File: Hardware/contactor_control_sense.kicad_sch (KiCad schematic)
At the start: 52 parts, among them J10 ContactorConnector, J11 ContactorConnector, J4 ContactorConnector, J9 ContactorConnector, Q4 PSMN8R5-40MSDX, Q5 PSMN8R5-40MSDX, Q6 PSMN8R5-40MSDX, Q7 PSMN8R5-40MSDX, SW3 SW_Push_Open, SW4 SW_Push_Open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

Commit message: BPS-Leader Schematic completed (mostly)
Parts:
- removed R31, R35, R42: 10k, Resistor_SMD:R_0603_1608Metric, symbol Device:R_US
- removed SW3, SW4, SW5, SW6: SW_Push_Open, symbol Switch:SW_Push_Open
- added J12, J14, J15: Conn_01x02, symbol Connector_Generic:Conn_01x02
- added Q10, Q8, Q9: PMV213SN,215, Package_TO_SOT_SMD:SOT-23-3, symbol Transistor_FET:BUK7M27-80EX
- added R50, R54: 10k, Resistor_SMD:R_0603_1608Metric, symbol Device:R_US
- D5, D6, D8, D9: footprint UTSVT_Passive:MMDL101T1G -> UTSVT_Passives:MMDL101T1G
- Q4, Q5, Q6, Q7: value PSMN8R5-40MSDX -> PMV213SN,215; footprint Package_TO_SOT_SMD:LFPAK33 -> Package_TO_SOT_SMD:SOT-23-3
- renumbered HV+ to HV+4
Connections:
- net +24V: now also J12.1 (Pin_1); no longer D6.1 (K), R32.2
- net +3.3V: now also Q7.5 (D), Q10.5 (D), Q8.5 (D)
- net ARRAY_CONTROL: now also R29.2, Q9.4 (G); no longer R43.2
- net ARRAY_PRE_CONTROL: now also Q4.4 (G), R39.2
- net GND: now also R43.2, Q9.1 (S), Q9.2 (S), Q9.3 (S), R50.2, R54.2; no longer Q7.1 (S), Q7.2 (S), Q7.3 (S), R43.1
- net HV+_CONTROL: now also Q5.4 (G), R44.2
- net HV-_CONTROL: now also Q6.4 (G), R45.2
- net at Q7.4 (G): now also D6.1 (K), R32.2, J15.2 (Pin_2); no longer R39.2
- net ARRAY_PRE_SENSE- renamed ARRAY_PRE_CONTROL-
- net ARRAY_PRE_CONTROL-: now also Q4.5 (D); no longer Q7.5 (D)
- net ARRAY_SENSE- renamed ARRAY_CONTROL-
- net ARRAY_CONTROL-: now also Q9.5 (D); no longer Q4.5 (D)
- net HV+_SENSE- renamed HV+_CONTROL-
- net HV-_SENSE- renamed HV-_CONTROL-
- new net: J12.2 (Pin_2), J14.1 (Pin_1), Q10.4 (G)
- new net: J14.2 (Pin_2), J15.1 (Pin_1), Q8.4 (G)
- new net ESTOP_1: Q10.1 (S), Q10.2 (S), Q10.3 (S), R43.1
- new net ESTOP_2: Q8.1 (S), Q8.2 (S), Q8.3 (S), R50.1
- new net ESTOP_3: Q7.1 (S), Q7.2 (S), Q7.3 (S), R54.1
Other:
- note removed: "I was recently informed that this may have to go on 4 seperate sheets In addition, I fear I might have implemented "estop button in series" too literally"
- moved on the sheet: C15, C16, C17, C19, C22, C23, D6, D8, D9, HV+1, HV+2, HV+3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

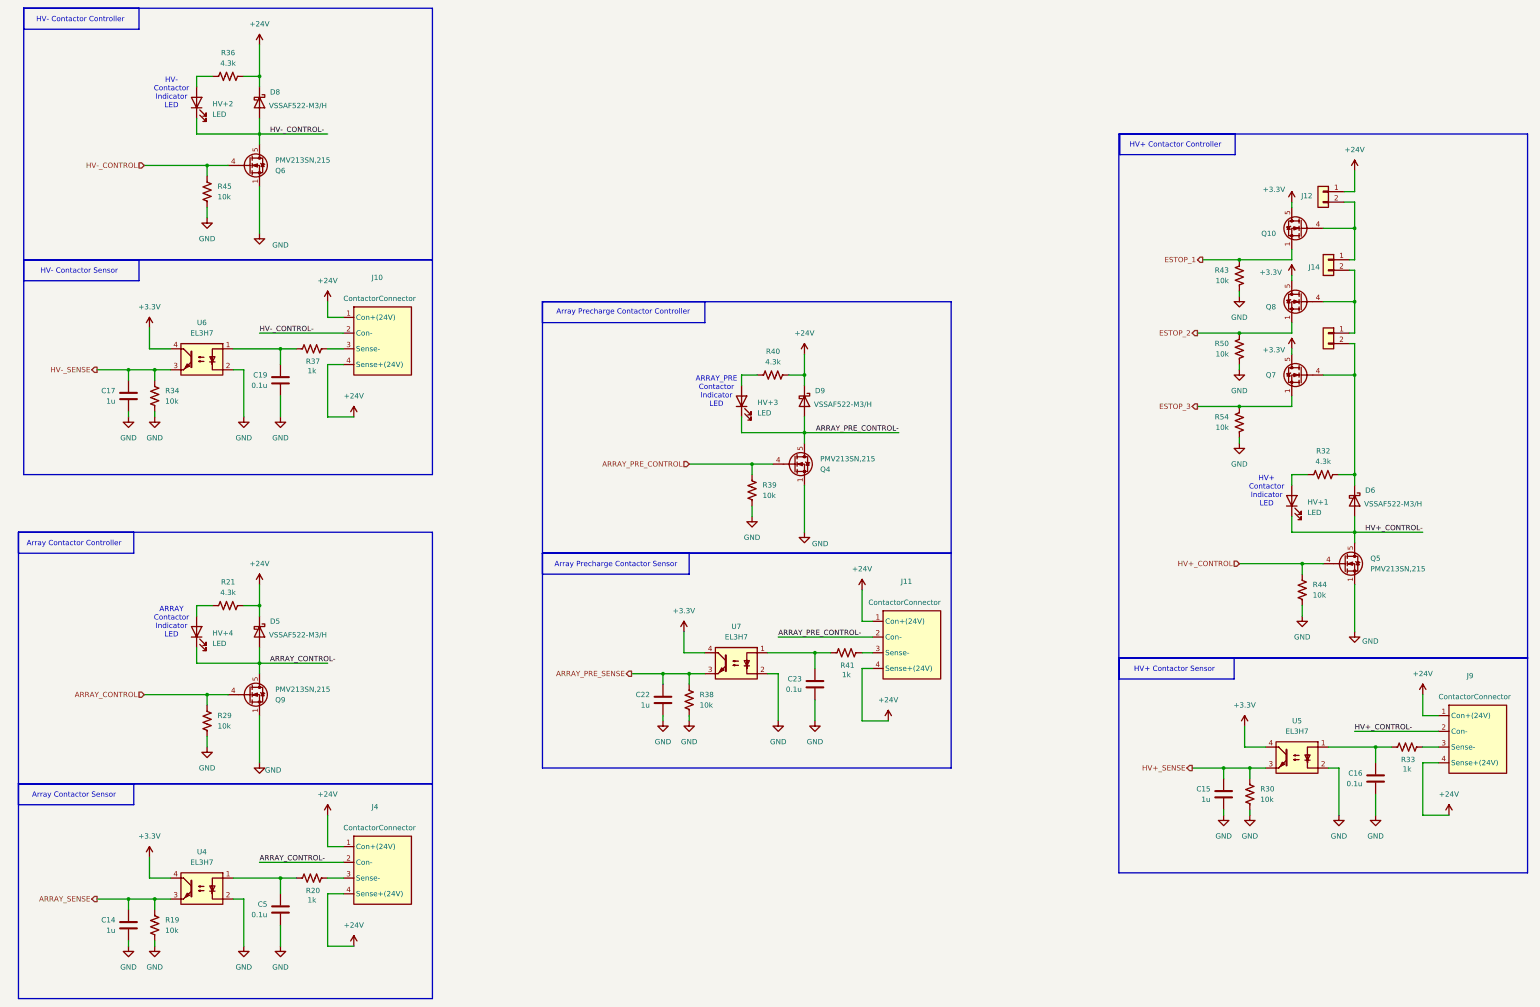
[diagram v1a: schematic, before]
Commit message: added fuse, made kiCad Sharepoint a submodule, added a pulldown, added test-points
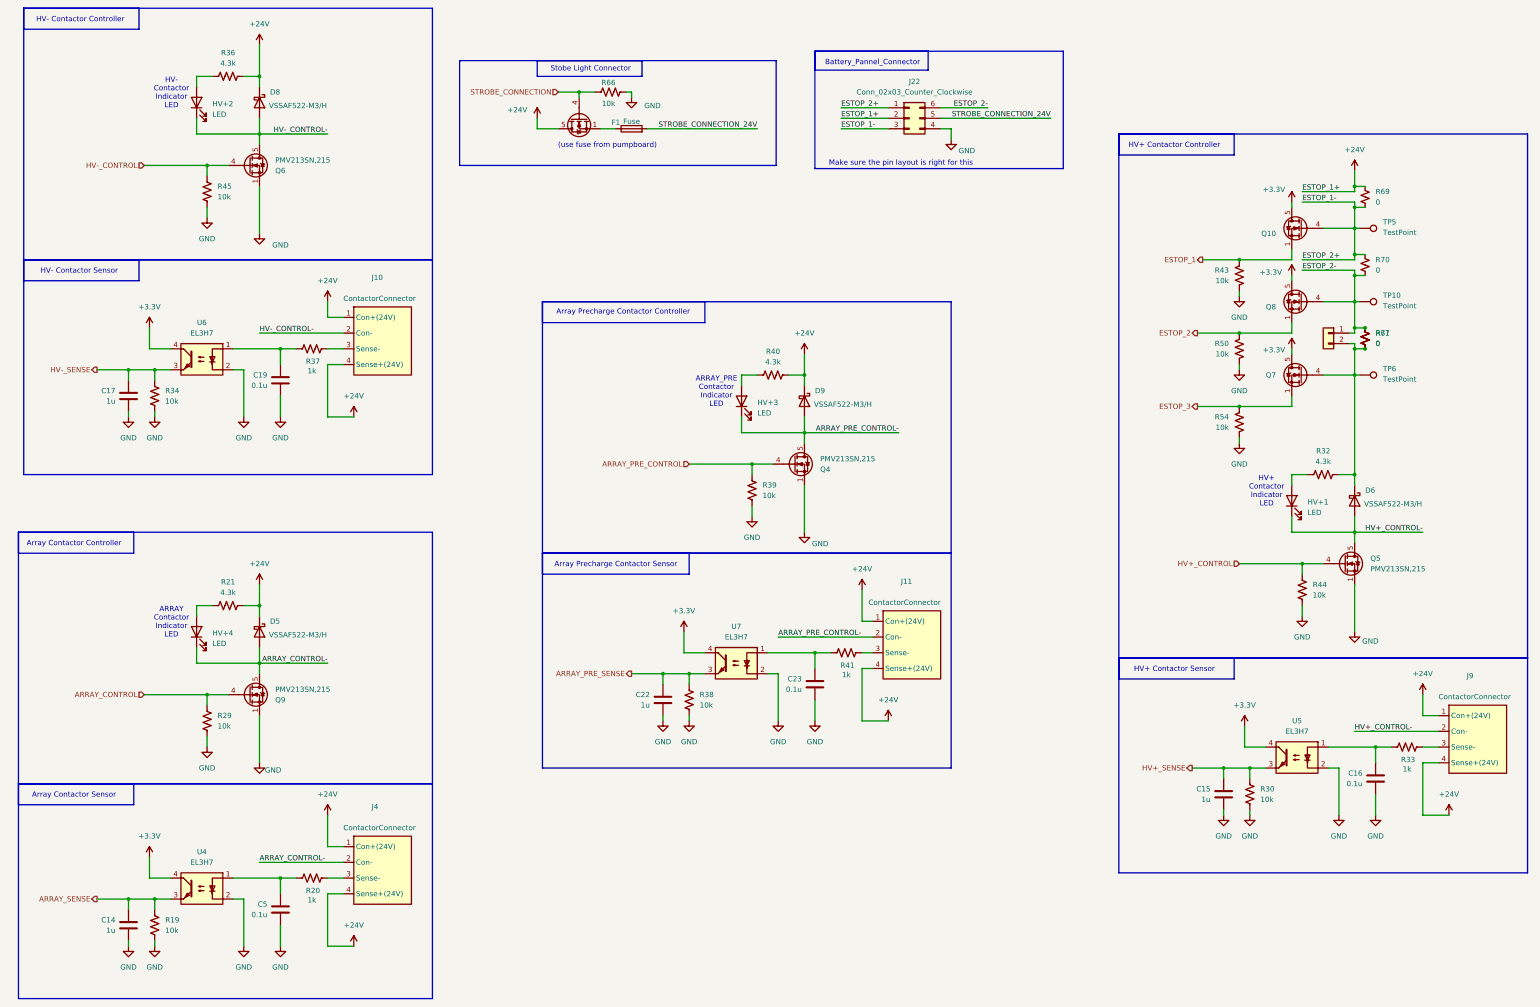
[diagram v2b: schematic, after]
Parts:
- removed J12, J14: Conn_01x02, symbol Connector_Generic:Conn_01x02
- added F1: Fuse, symbol Device:Fuse
- added J22: Conn_02x03_Counter_Clockwise, symbol Connector_Generic:Conn_02x03_Counter_Clockwise
- added Q11: PMV213SN,215, Package_TO_SOT_SMD:SOT-23-3, symbol Transistor_FET:BUK7M27-80EX
- added R66: 10k, Resistor_SMD:R_0603_1608Metric, symbol Device:R_US
- added R67, R69, R70, R71: 0, symbol Device:R_Small_US
- added TP10, TP5, TP6: TestPoint, symbol Connector:TestPoint
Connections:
- net +24V: now also J22.2 (Pin_2), Q11.5 (D), R69.1
- net GND: now also J22.4 (Pin_4), R66.2
- net ESTOP_1-: now reaches Q10.4 (G)
- net ESTOP_1-: now also J22.1 (Pin_1), J22.3 (Pin_3), R69.2, R70.1, TP5.1
- net at D6.1 (K), J15.2 (Pin_2), Q7.4 (G)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: now also R67.2, R71.2, TP6.1
- net ESTOP_2-: now reaches J15.1 (Pin_1), Q8.4 (G)
- net ESTOP_2-: now also J22.6 (Pin_6), R67.1, R70.2, R71.1, TP10.1
- new net: F1.1, Q11.1 (S), Q11.2 (S), Q11.3 (S)
- new net STROBE_CONNECTION: Q11.4 (G), R66.1
- new net STROBE_CONNECTION_24V: F1.2, J22.5 (Pin_5)
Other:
- note added: "(use fuse from pumpboard)"
- note added: "Battery_Pannel_Connector"
- note added: "Make sure the pin layout is right for this"
- note added: "Stobe Light Connector"

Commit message: Small tweaks
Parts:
- removed R67: 0, symbol Device:R_Small_US
- added TP34, TP36, TP37, TP38, TP39, TP40, TP41, TP42, TP43, TP44, TP45, TP7, TP8, TP9: TestPoint, UTSVT_Special:TestPoint_HEX_3mmID, symbol Connector:TestPoint
- R69, R70, R71: footprint (none) -> Resistor_SMD:R_0603_1608Metric; now not fitted
- TP10, TP5, TP6: footprint (none) -> UTSVT_Special:TestPoint_HEX_3mmID
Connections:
- net ARRAY_CONTROL: now also TP38.1
- net ARRAY_CONTROL-: now also TP34.1
- net ARRAY_PRE_CONTROL: now also TP42.1
- net ARRAY_PRE_CONTROL-: now also TP9.1
- net ARRAY_PRE_SENSE: now also TP41.1
- net ARRAY_SENSE: now also TP40.1
- net HV+_CONTROL: now also TP45.1, TP8.1
- net HV+_CONTROL-: now also TP7.1
- net HV+_SENSE: now also TP44.1
- net HV-_CONTROL: now also TP39.1
- net HV-_CONTROL-: now also TP36.1
- net HV-_SENSE: now also TP37.1
- net STROBE_CONNECTION_24V: now also TP43.1
- net ESTOP_1- renamed ESTOP_1-,2+
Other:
- moved on the sheet: Q10, Q7, Q8

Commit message: Very, very intial layout designed. Many issues. Too bad!
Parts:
- removed F1: Fuse, symbol Device:Fuse
- removed J22: Conn_02x03_Counter_Clockwise, symbol Connector_Generic:Conn_02x03_Counter_Clockwise
- removed Q11: PMV213SN,215, Package_TO_SOT_SMD:SOT-23-3, symbol Transistor_FET:BUK7M27-80EX
- removed R66: 10k, Resistor_SMD:R_0603_1608Metric, symbol Device:R_US
- removed TP43, TP8: TestPoint, UTSVT_Special:TestPoint_HEX_3mmID, symbol Connector:TestPoint
- J15: footprint (none) -> Connector_Molex:Molex_Nano-Fit_105309-xx02_1x02_P2.50mm_Vertical
- TP10, TP34, TP36, TP37, TP38, TP39, TP40, TP41, TP42, TP44, TP45, TP5, TP6, TP7, TP9: footprint UTSVT_Special:TestPoint_HEX_3mmID -> TestPoint:TestPoint_Pad_1.0x1.0mm
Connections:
- net ESTOP_1 renamed ESTOP_1_SENSE
- net ESTOP_1-,2+ renamed ESTOP_1-/2+
- net ESTOP_2 renamed ESTOP_2_SENSE
- net ESTOP_3 renamed ESTOP_3_SENSE
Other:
- note removed: "(use fuse from pumpboard)"
- note removed: "Battery_Pannel_Connector"
- note removed: "Make sure the pin layout is right for this"
- note removed: "Stobe Light Connector"

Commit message: Backup
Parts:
- J15: footprint Connector_Molex:Molex_Nano-Fit_105309-xx02_1x02_P2.50mm_Vertical -> UTSVT_Connectors:Molex_Nano-Fit_105309-xx02_1x02_P2.50mm_Vertical
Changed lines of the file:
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@@
 			)
 		)
-		(property "Footprint" "Connector_Molex:Molex_Nano-Fit_105309-xx02_1x02_P2.50mm_Vertical"
+		(property "Footprint" "UTSVT_Connectors:Molex_Nano-Fit_105309-xx02_1x02_P2.50mm_Vertical"
 			(at 334.01 96.52 0)
 			(effects

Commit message: small fixes
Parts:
- C14, C15, C17, C22: P/N (none) -> C0805C105K5PACTU
- C16, C19, C23, C5: Manufactuerer (none) -> TAIYO YUDEN; P/N (none) -> MLASH168SB7104KTNA01
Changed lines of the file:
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@@
 			)
 		)
-		(property "Datasheet" "~"
+		(property "Datasheet" "https://ds.yuden.co.jp/TYCOMPAS/or/download?pn=MLAST063SCG681JFNA01&fileType=CA"
 			(at 209.55 181.61 0)
 			(effects
@@
 			)
 		)
-		(property "Manufactuerer" ""
+		(property "Manufactuerer" "TAIYO YUDEN "
+			(at 209.55 181.61 0)
+			(effects
+				(font
+					(size 1.27 1.27)
+				)
+				(hide yes)
+			)
+		)
+		(property "P/N" "MLASH168SB7104KTNA01 "
 			(at 209.55 181.61 0)
 			(effects
@@
 			)
 		)
+		(property "P/N" "C0805C105K5PACTU"
+			(at 43.18 240.03 0)
+			(effects
+				(font
+					(size 1.27 1.27)
+				)
+				(hide yes)
+			)
+		)
 		(pin "2"
 		)
@@
 			)
 		)
+		(property "P/N" "C0805C105K5PACTU"
+			(at 308.61 208.28 0)
+			(effects
+				(font
+					(size 1.27 1.27)
+				)
+				(hide yes)
+			)
+		)
 		(pin "2"
 		)
@@
 			)
 		)
+		(property "P/N" "C0805C105K5PACTU"
+			(at 172.72 185.42 0)
+			(effects
+				(font
+					(size 1.27 1.27)
+				)
+				(hide yes)
+			)
+		)
 		(pin "2"
 		)
@@
 			)
 		)
-		(property "Datasheet" "~"
+		(property "Datasheet" "https://ds.yuden.co.jp/TYCOMPAS/or/download?pn=MLAST063SCG681JFNA01&fileType=CA"
 			(at 80.01 107.95 0)
 			(effects
@@
 			)
 		)
-		(property "Manufactuerer" ""
+		(property "Manufactuerer" "TAIYO YUDEN "
+			(at 80.01 107.95 0)
+			(effects
+				(font
+					(size 1.27 1.27)
+				)
+				(hide yes)
+			)
+		)
+		(property "P/N" "MLASH168SB7104KTNA01 "
 			(at 80.01 107.95 0)
 			(effects
@@
 			)
 		)
-		(property "Datasheet" "~"
+		(property "Datasheet" "https://ds.yuden.co.jp/TYCOMPAS/or/download?pn=MLAST063SCG681JFNA01&fileType=CA"
 			(at 80.01 236.22 0)
 			(effects
@@
 			)
 		)
-		(property "Manufactuerer" ""
+		(property "Manufactuerer" "TAIYO YUDEN "
+			(at 80.01 236.22 0)
+			(effects
+				(font
+					(size 1.27 1.27)
+				)
+				(hide yes)
+			)
+		)
+		(property "P/N" "MLASH168SB7104KTNA01 "
 			(at 80.01 236.22 0)
 			(effects
@@
 			)
 		)
+		(property "P/N" "C0805C105K5PACTU"
+			(at 43.18 111.76 0)
+			(effects
+				(font
+					(size 1.27 1.27)
+				)
+				(hide yes)
+			)
+		)
 		(pin "2"
 		)
@@
 			)
 		)
-		(property "Datasheet" "~"
+		(property "Datasheet" "https://ds.yuden.co.jp/TYCOMPAS/or/download?pn=MLAST063SCG681JFNA01&fileType=CA"
 			(at 345.44 204.47 0)
 			(effects
@@
 			)
 		)
-		(property "Manufactuerer" ""
+		(property "Manufactuerer" "TAIYO YUDEN "
+			(at 345.44 204.47 0)
+			(effects
+				(font
+					(size 1.27 1.27)
+				)
+				(hide yes)
+			)
+		)
+		(property "P/N" "MLASH168SB7104KTNA01 "
 			(at 345.44 204.47 0)
 			(effects
